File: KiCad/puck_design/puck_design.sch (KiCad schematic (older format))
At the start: 28 parts, among them J1 SJ-2523-SMT-TR, Q1 CSD16406Q3, Q2 CSD16406Q3, U1 ITG-3701, U2 BT840F, U3 TE832-M1, U4 MCP73832-2, U5 BQ29700DSER

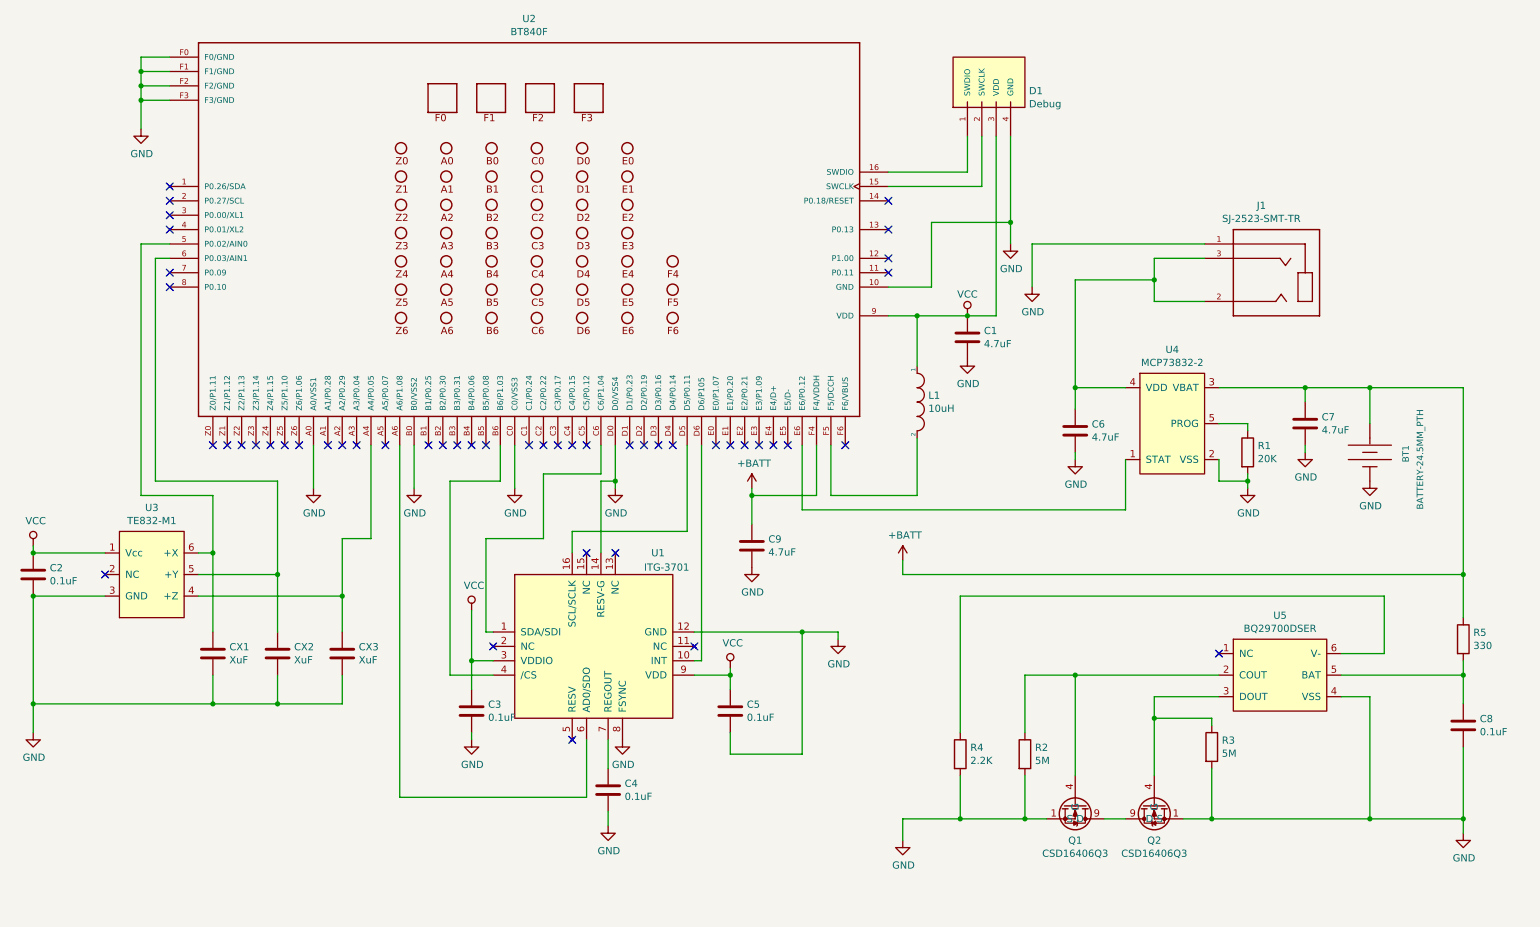
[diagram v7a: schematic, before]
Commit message: Added mounting holes and updated gerber/drill files
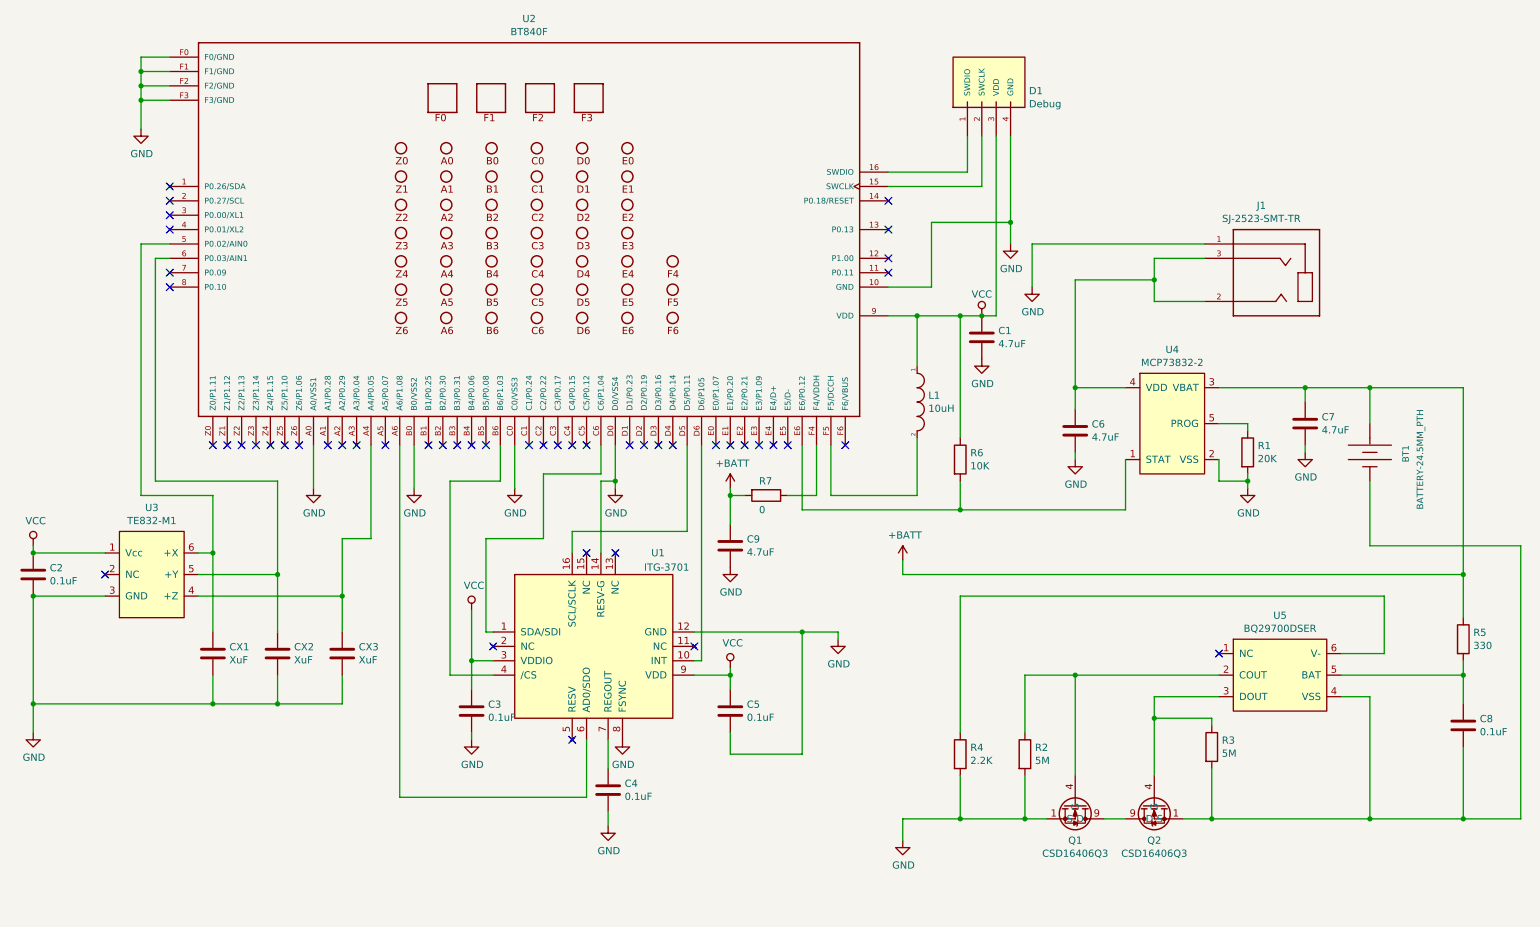
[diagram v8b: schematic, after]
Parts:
- added R6: 10K, puck_footprints:0805-NO, symbol Device:R
- added R7: 0, puck_footprints:0805-NO, symbol Device:R
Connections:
- net +BATT: now also R7.2; no longer U2.F4 (F4/VDDH)
- net GND: no longer BT1.2 (-), C8.2, Q2.1 (S), Q2.2 (S), Q2.3 (S), R3.2, U5.4 (VSS)
- net VCC: now also R6.1
- net at U2.E6 (E6/P0.12), U4.1 (STAT): now also R6.2
- new net: R7.1, U2.F4 (F4/VDDH)
- new net: BT1.2 (-), C8.2, Q2.1 (S), Q2.2 (S), Q2.3 (S), R3.2, U5.4 (VSS)
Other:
- moved on the sheet: C1, C9
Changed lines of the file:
@@
 L Device:C C1
 U 1 1 5C0A4E4C
-P 7200 2800
-F 0 "C1" H 7315 2846 50  0000 L CNN
-F 1 "4.7uF" H 7315 2755 50  0000 L CNN
-F 2 "puck_footprints:CAPC2012X140N" H 7238 2650 50  0001 C CNN
-F 3 "~" H 7200 2800 50  0001 C CNN
-	1    7200 2800
+P 7300 2800
+F 0 "C1" H 7415 2846 50  0000 L CNN
+F 1 "4.7uF" H 7415 2755 50  0000 L CNN
+F 2 "puck_footprints:CAPC2012X140N" H 7338 2650 50  0001 C CNN
+F 3 "~" H 7300 2800 50  0001 C CNN
+	1    7300 2800
 	1    0    0    -1
 $EndComp
@@
 L power:VCC #PWR0105
 U 1 1 5C1F6E15
-P 7200 2650
-F 0 "#PWR0105" H 7200 2500 50  0001 C CNN
-F 1 "VCC" H 7200 2800 50  0000 C CNN
-F 2 "" H 7200 2650 50  0001 C CNN
-F 3 "" H 7200 2650 50  0001 C CNN
-	1    7200 2650
+P 7300 2650
+F 0 "#PWR0105" H 7300 2500 50  0001 C CNN
+F 1 "VCC" H 7300 2800 50  0000 C CNN
+F 2 "" H 7300 2650 50  0001 C CNN
+F 3 "" H 7300 2650 50  0001 C CNN
+	1    7300 2650
 	1    0    0    -1
 $EndComp
@@
 	1    0    0    -1
 $EndComp
-Connection ~ 7200 2650
 Wire Wire Line
 	8950 3150 9550 3150
@@
 L Device:C C9
 U 1 1 5C4737B3
-P 5700 4250
-F 0 "C9" H 5815 4296 50  0000 L CNN
-F 1 "4.7uF" H 5815 4205 50  0000 L CNN
-F 2 "puck_footprints:CAPC2012X140N" H 5738 4100 50  0001 C CNN
-F 3 "~" H 5700 4250 50  0001 C CNN
-	1    5700 4250
-	1    0    0    -1
-$EndComp
-Wire Wire Line
-	5700 4100 5700 3900
+P 5550 4250
+F 0 "C9" H 5665 4296 50  0000 L CNN
+F 1 "4.7uF" H 5665 4205 50  0000 L CNN
+F 2 "puck_footprints:CAPC2012X140N" H 5588 4100 50  0001 C CNN
+F 3 "~" H 5550 4250 50  0001 C CNN
+	1    5550 4250
+	1    0    0    -1
+$EndComp
 Wire Wire Line
 	6650 2650 6850 2650
@@
 	6850 3000 6850 2650
 Connection ~ 6850 2650
-Wire Wire Line
-	6850 2650 7200 2650
 $Comp
 L power:+BATT #PWR0102
@@
 L power:+BATT #PWR0103
 U 1 1 5C50F1C9
-P 5700 3850
-F 0 "#PWR0103" H 5700 3700 50  0001 C CNN
-F 1 "+BATT" H 5715 4023 50  0000 C CNN
-F 2 "" H 5700 3850 50  0001 C CNN
-F 3 "" H 5700 3850 50  0001 C CNN
-	1    5700 3850
-	1    0    0    -1
-$EndComp
-Wire Wire Line
-	6150 3900 5700 3900
+P 5550 3850
+F 0 "#PWR0103" H 5550 3700 50  0001 C CNN
+F 1 "+BATT" H 5565 4023 50  0000 C CNN
+F 2 "" H 5550 3850 50  0001 C CNN
+F 3 "" H 5550 3850 50  0001 C CNN
+	1    5550 3850
+	1    0    0    -1
+$EndComp
 Wire Wire Line
 	6150 3550 6150 3900
-Connection ~ 5700 3900
-Wire Wire Line
-	5700 3900 5700 3850
 Wire Wire Line
 	6250 3900 6850 3900
 Wire Wire Line
 	6250 3550 6250 3900
-Wire Wire Line
-	6850 3500 6850 3900
 $Comp
 L puck_library:SJ-2523-SMT-TR J1
@@
 	3250 6000 4550 6000
 Wire Wire Line
-	8300 4000 6050 4000
+	8300 4000 7150 4000
 Wire Wire Line
 	6050 4000 6050 3550
@@
 Connection ~ 10000 3150
 Connection ~ 10650 4450
-$Comp
-L power:GND #PWR0101
-U 1 1 5C4B69D4
-P 10000 3800
-F 0 "#PWR0101" H 10000 3550 50  0001 C CNN
-F 1 "GND" H 10005 3627 50  0000 C CNN
-F 2 "" H 10000 3800 50  0001 C CNN
-F 3 "" H 10000 3800 50  0001 C CNN
-	1    10000 3800
-	1    0    0    -1
-$EndComp
-$Comp
-L power:GND #PWR0106
-U 1 1 5C4BC67D
-P 10650 6250
-F 0 "#PWR0106" H 10650 6000 50  0001 C CNN
-F 1 "GND" H 10655 6077 50  0000 C CNN
-F 2 "" H 10650 6250 50  0001 C CNN
-F 3 "" H 10650 6250 50  0001 C CNN
-	1    10650 6250
-	1    0    0    -1
-$EndComp
-Wire Wire Line
-	10650 6250 10650 6150
-Connection ~ 10650 6150
 Wire Wire Line
 	7950 3150 8300 3150
@@
 L power:GND #PWR0108
 U 1 1 5C4E6BFD
-P 7200 2950
-F 0 "#PWR0108" H 7200 2700 50  0001 C CNN
-F 1 "GND" H 7205 2777 50  0000 C CNN
-F 2 "" H 7200 2950 50  0001 C CNN
-F 3 "" H 7200 2950 50  0001 C CNN
-	1    7200 2950
+P 7300 2950
+F 0 "#PWR0108" H 7300 2700 50  0001 C CNN
+F 1 "GND" H 7305 2777 50  0000 C CNN
+F 2 "" H 7300 2950 50  0001 C CNN
+F 3 "" H 7300 2950 50  0001 C CNN
+	1    7300 2950
 	1    0    0    -1
 $EndComp
@@
 L power:GND #PWR0111
 U 1 1 5C4F2BFA
-P 5700 4400
-F 0 "#PWR0111" H 5700 4150 50  0001 C CNN
-F 1 "GND" H 5705 4227 50  0000 C CNN
-F 2 "" H 5700 4400 50  0001 C CNN
-F 3 "" H 5700 4400 50  0001 C CNN
-	1    5700 4400
+P 5550 4400
+F 0 "#PWR0111" H 5550 4150 50  0001 C CNN
+F 1 "GND" H 5555 4227 50  0000 C CNN
+F 2 "" H 5550 4400 50  0001 C CNN
+F 3 "" H 5550 4400 50  0001 C CNN
+	1    5550 4400
 	1    0    0    -1
 $EndComp
@@
 $EndComp
 Wire Wire Line
-	7200 2650 7400 2650
-Wire Wire Line
 	6650 1650 7200 1650
 Wire Wire Line
@@
 Wire Wire Line
 	6950 2000 7500 2000
+Wire Wire Line
+	10000 3800 10000 4250
+Wire Wire Line
+	10000 4250 11050 4250
+Wire Wire Line
+	11050 4250 11050 6150
+Wire Wire Line
+	11050 6150 10650 6150
+Connection ~ 10650 6150
+Connection ~ 7300 2650
+Wire Wire Line
+	7300 2650 7400 2650
+Wire Wire Line
+	6850 2650 7150 2650
+$Comp
+L Device:R R6
+U 1 1 5C773CAB
+P 7150 3650
+F 0 "R6" H 7220 3696 50  0000 L CNN
+F 1 "10K" H 7220 3605 50  0000 L CNN
+F 2 "puck_footprints:0805-NO" V 7080 3650 50  0001 C CNN
+F 3 "~" H 7150 3650 50  0001 C CNN
+	1    7150 3650
+	1    0    0    -1
+$EndComp
+Wire Wire Line
+	7150 3500 7150 2650
+Connection ~ 7150 2650
+Wire Wire Line
+	7150 2650 7300 2650
+Wire Wire Line
+	7150 3800 7150 4000
+Wire Wire Line
+	6850 3500 6850 3900
+Connection ~ 7150 4000
+Wire Wire Line
+	7150 4000 6050 4000
+Wire Wire Line
+	5550 3850 5550 3900
+$Comp
+L Device:R R7
+U 1 1 5C798B7E
+P 5800 3900
+F 0 "R7" V 5700 3850 50  0000 L CNN
+F 1 "0" V 5900 3850 50  0000 L CNN
+F 2 "puck_footprints:0805-NO" V 5730 3900 50  0001 C CNN
+F 3 "~" H 5800 3900 50  0001 C CNN
+	1    5800 3900
+	0    1    1    0
+$EndComp
+Wire Wire Line
+	5650 3900 5550 3900
+Connection ~ 5550 3900
+Wire Wire Line
+	5550 3900 5550 4100
+Wire Wire Line
+	6150 3900 5950 3900
 $EndSCHEMATC
